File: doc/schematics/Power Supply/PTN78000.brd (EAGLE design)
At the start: 160 x 100 mm, 5 parts, among them U1 1.5APOWERMODULE

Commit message: New schematics
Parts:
- removed C4: (no value), rcl:C1206
- removed C5: (no value), rcl:E5-6
- removed U1: 1.5APOWERMODULE, TIPOWERMODULE:1.5APOWERMODULE
- removed X: OUTPUT (6 V), con-wago-500:W237-102
- added C1: 2.2 uF, ASL:1206
- added C2: 100 uF, ASL:1206
- added F1: FUSE, ASL:FUSE_2AG
- added J11, J13, J14, J15, J16, J9: POW_CONNECTFEMALE-RA, ASL:SOCKET-FEMALE_RA-3.96MM-2
- added JP1: M03PTH, ASL:1X03
- added LED1: (no value), SparkFun-LED:LED5MM
- added R2: 330, ASL:1206
- added U$1: PTN78000THROUGH-HOLE, ASL:PTN78000
- R1: value 13.1 K -> 21 K; device rcl:0207/10 -> ASL:1206
- moved R1 23.0 mm to (25.4, 35.6), turned to 90 degrees
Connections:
- removed net VCC: U1.P$2
- new net N$4: JP1.3, U$1.INHIBIT
- new net N$5: C2.1, F1.P$1, F1.P$2, U$1.V_OUT
- new net N$6: LED1.A, R2.2
- new net VCC5V0: F1.P$3, F1.P$4, J11.1, J13.1, J14.1, J15.1, J16.1, J9.1, R2.1
- net GND: now also C1.2, C2.2, J11.2, J13.2, J14.2, J15.2, J16.2, J9.2, JP1.2, LED1.K, R1.2, U$1.GND; no longer C4.2, C5.-, R1.1, U1.P$1
- net N$1: now also C1.1, JP1.1, U$1.V_IN; no longer R1.2, U1.P$4
- net N$2: now also R1.1, U$1.ADJ; no longer C4.1, C5.+, U1.P$5, X.2
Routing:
- net N$3: track 155.9 -> 0.00 mm
- net GND: track 0.00 -> 128.2 mm, vias 0 -> 1
- net VCC5V0: track 0.00 -> 105.0 mm
- net N$5: track 0.00 -> 16.4 mm, vias 1 -> 0
- net N$4: track 0.00 -> 9.68 mm, vias 1 -> 0
- net N$6: track 0.00 -> 5.33 mm, vias 1 -> 0
- net N$2: track 0.00 -> 4.76 mm
- net N$1: track 4.37 -> 9.00 mm
- added copper zone on layer 16, net GND
- added copper zone on layer 1, net VCC5V0
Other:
- board size 160 x 100 mm -> 51.7 x 36.8 mm

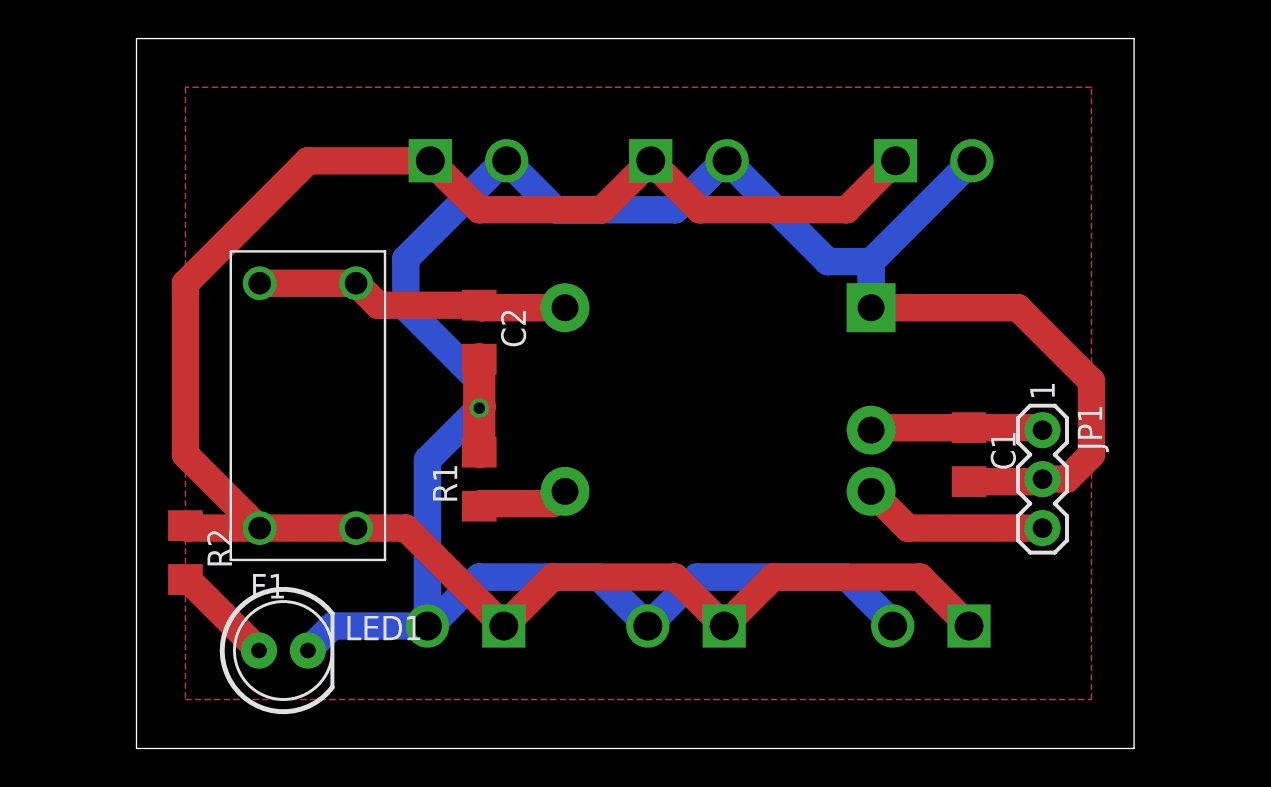
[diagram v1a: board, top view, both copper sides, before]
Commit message: Schematic updates
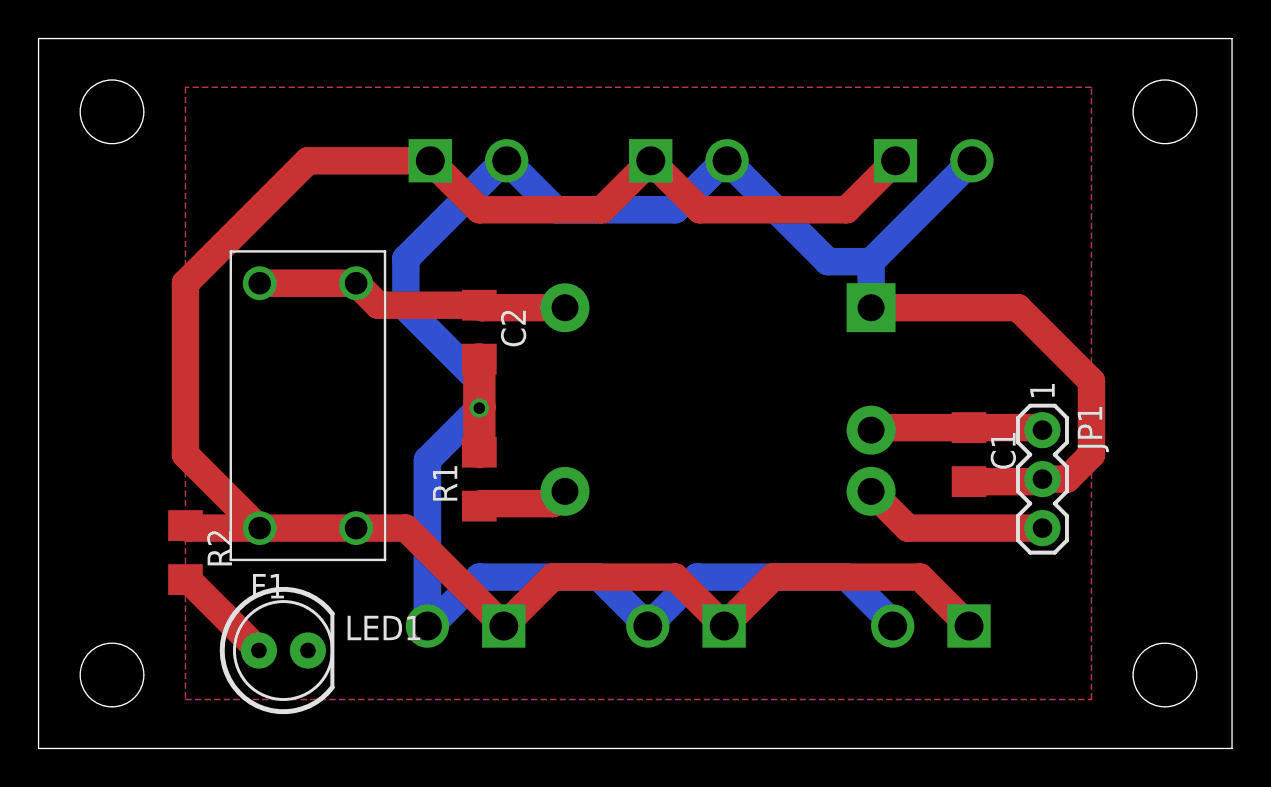
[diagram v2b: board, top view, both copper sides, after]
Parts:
- added U$11, U$12, U$13, U$6: (no value), ASL:STAND-OFF
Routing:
- net GND: track 128.2 -> 121.4 mm
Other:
- board size 51.7 x 36.8 mm -> 61.9 x 36.8 mm
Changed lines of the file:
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@@
 <layers>
 <layer number="1" name="Top" color="4" fill="1" visible="yes" active="yes"/>
-<layer number="16" name="Bottom" color="1" fill="1" visible="no" active="yes"/>
+<layer number="16" name="Bottom" color="1" fill="1" visible="yes" active="yes"/>
 <layer number="17" name="Pads" color="2" fill="1" visible="yes" active="yes"/>
 <layer number="18" name="Vias" color="2" fill="1" visible="yes" active="yes"/>
@@
 <board>
 <plain>
-<wire x1="7.62" y1="21.59" x2="59.36" y2="21.59" width="0" layer="20"/>
-<wire x1="59.36" y1="21.59" x2="59.36" y2="58.41" width="0" layer="20"/>
-<wire x1="59.36" y1="58.41" x2="7.62" y2="58.41" width="0" layer="20"/>
-<wire x1="7.62" y1="58.41" x2="7.62" y2="21.59" width="0" layer="20"/>
+<wire x1="2.54" y1="21.59" x2="64.44" y2="21.59" width="0" layer="20"/>
+<wire x1="64.44" y1="21.59" x2="64.44" y2="58.41" width="0" layer="20"/>
+<wire x1="64.44" y1="58.41" x2="2.54" y2="58.41" width="0" layer="20"/>
+<wire x1="2.54" y1="58.41" x2="2.54" y2="21.59" width="0" layer="20"/>
 </plain>
 <attributes>
@@
 <element name="R2" library="ASL" package="1206" value="330" x="10.16" y="31.75" rot="R270"/>
 <element name="LED1" library="SparkFun-LED" package="LED5MM" value="" x="15.24" y="26.67"/>
+<element name="U$6" library="ASL" package="STAND-OFF" value="" x="6.35" y="25.4"/>
+<element name="U$11" library="ASL" package="STAND-OFF" value="" x="6.35" y="54.61"/>
+<element name="U$12" library="ASL" package="STAND-OFF" value="" x="60.96" y="54.61"/>
+<element name="U$13" library="ASL" package="STAND-OFF" value="" x="60.96" y="25.4"/>
 </elements>
 <signals>
@@
 <wire x1="25.4" y1="39.37" x2="25.4" y2="39.243" width="1.6764" layer="1"/>
 <wire x1="25.4" y1="39.243" x2="25.4" y2="36.96" width="1.6764" layer="1"/>
-<via x="25.4" y="39.243" extent="1-16" drill="0.6"/>
+<via x="25.4" y="39.243" extent="1-16" drill="0.6" diameter="0.4064"/>
 <contactref element="LED1" pad="K"/>
 <wire x1="50.8" y1="35.43" x2="54.48" y2="35.43" width="1.4224" layer="1"/>
@@
 <wire x1="25.4" y1="40.64" x2="25.4" y2="39.243" width="1.4224" layer="16"/>
 <wire x1="25.4" y1="36.96" x2="25.4" y2="39.37" width="1.4224" layer="1"/>
-<wire x1="22.71" y1="27.94" x2="17.78" y2="27.94" width="1.4224" layer="16"/>
-<wire x1="17.78" y1="27.94" x2="16.51" y2="26.67" width="1.4224" layer="16"/>
 <wire x1="22.71" y1="27.94" x2="22.71" y2="36.553" width="1.4224" layer="16"/>
 <wire x1="22.71" y1="36.553" x2="25.4" y2="39.243" width="1.4224" layer="16"/>
